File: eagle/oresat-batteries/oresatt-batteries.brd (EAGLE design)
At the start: 160 x 100 mm, 6 parts, among them U1 TCAN330

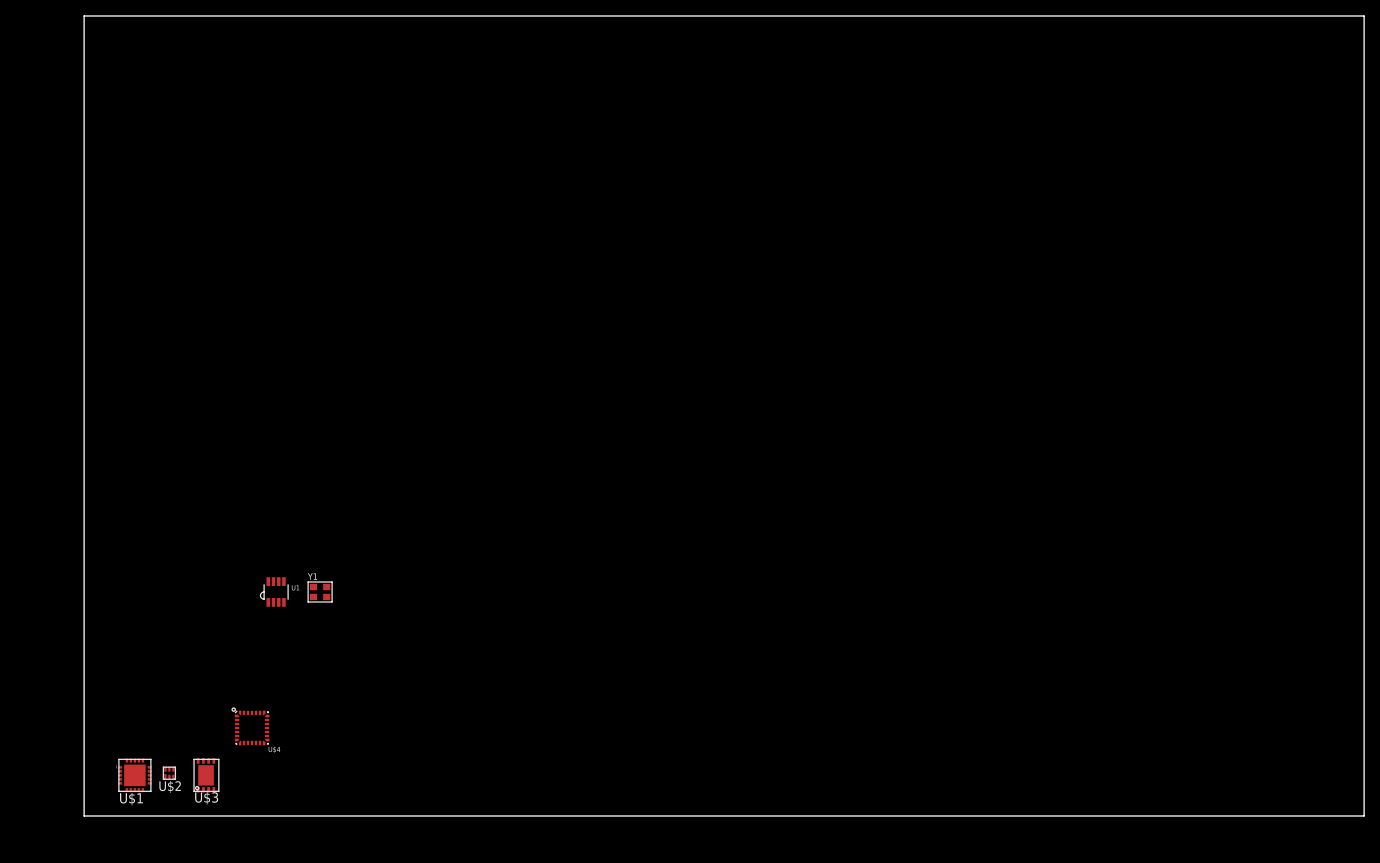
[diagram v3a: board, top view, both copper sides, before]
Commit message: Added 40 pin for real this time.
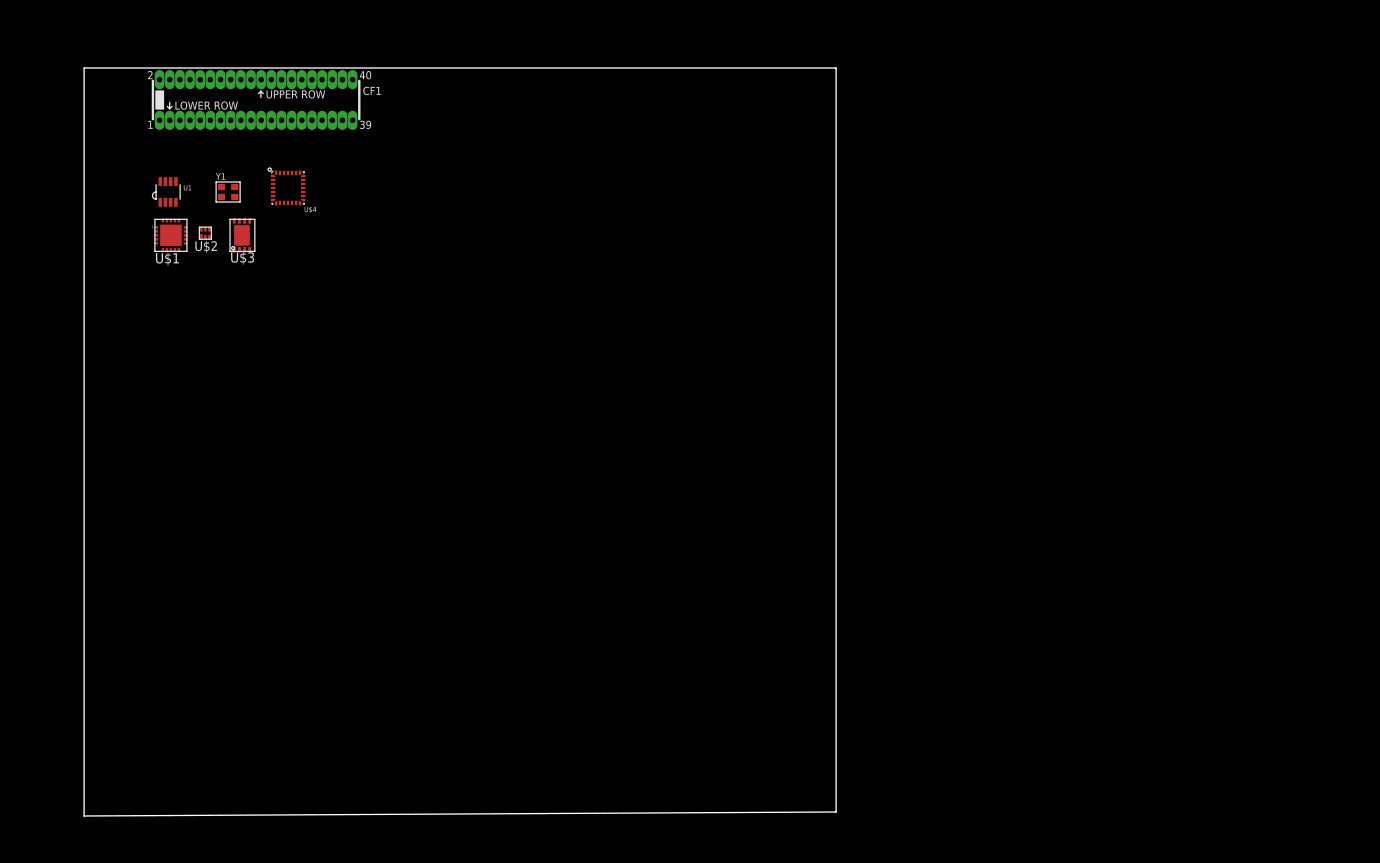
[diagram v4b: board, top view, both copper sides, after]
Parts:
- added CF1: ORESAT-CONNECTOR-40PIN, low-gain-radio:HARWIN-ARCHER-M50-3202045
- moved U$1 67.6 mm to (10.8, 72.6)
- moved U$2 67.6 mm to (15.2, 72.8)
- moved U$3 67.6 mm to (19.7, 72.6)
- moved U$4 67.6 mm to (25.5, 78.5)
- moved U1 51.8 mm to (10.5, 78.0)
- moved Y1 51.3 mm to (18.0, 78.0)
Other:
- board size 160 x 100 mm -> 94 x 93.5 mm
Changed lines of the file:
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@@
 <board>
 <plain>
-<wire x1="0" y1="0" x2="160" y2="0" width="0" layer="20"/>
-<wire x1="160" y1="0" x2="160" y2="100" width="0" layer="20"/>
-<wire x1="160" y1="100" x2="0" y2="100" width="0" layer="20"/>
-<wire x1="0" y1="100" x2="0" y2="0" width="0" layer="20"/>
+<wire x1="0" y1="0" x2="94" y2="0.5" width="0" layer="20"/>
+<wire x1="94" y1="0.5" x2="94" y2="93.5" width="0" layer="20"/>
+<wire x1="94" y1="93.5" x2="0" y2="93.5" width="0" layer="20"/>
+<wire x1="0" y1="93.5" x2="0" y2="0" width="0" layer="20"/>
 </plain>
 <attributes>
@@
 </autorouter>
 <elements>
-<element name="U$1" library="oresat-batteries" package="20_4X4_VVTQ" value="ADP5063" x="6.35" y="5.08"/>
-<element name="U$2" library="oresat-batteries" package="PSOP6" value="BQ2970" x="10.66" y="5.35"/>
-<element name="U$3" library="oresat-batteries" package="WDFN8_3X4" value="LC709203F" x="15.24" y="5.08"/>
-<element name="U$4" library="oresat-batteries" package="UFQFPN-28" value="STM32F042G" x="21" y="11"/>
-<element name="U1" library="oresat-batteries" package="SOT23-8_TI-DCN" value="TCAN330" x="24" y="28"/>
-<element name="Y1" library="low-gain-radio" package="CRYSTAL_2.5X2" value="" x="29.5" y="28"/>
+<element name="U$1" library="oresat-batteries" package="20_4X4_VVTQ" value="ADP5063" x="10.85" y="72.58"/>
+<element name="U$2" library="oresat-batteries" package="PSOP6" value="BQ2970" x="15.16" y="72.85"/>
+<element name="U$3" library="oresat-batteries" package="WDFN8_3X4" value="LC709203F" x="19.74" y="72.58"/>
+<element name="U$4" library="oresat-batteries" package="UFQFPN-28" value="STM32F042G" x="25.5" y="78.5"/>
+<element name="U1" library="oresat-batteries" package="SOT23-8_TI-DCN" value="TCAN330" x="10.5" y="78"/>
+<element name="Y1" library="low-gain-radio" package="CRYSTAL_2.5X2" value="" x="18" y="78"/>
+<element name="CF1" library="low-gain-radio" package="HARWIN-ARCHER-M50-3202045" value="ORESAT-CONNECTOR-40PIN" x="21.5" y="89.5"/>
 </elements>
 <signals>

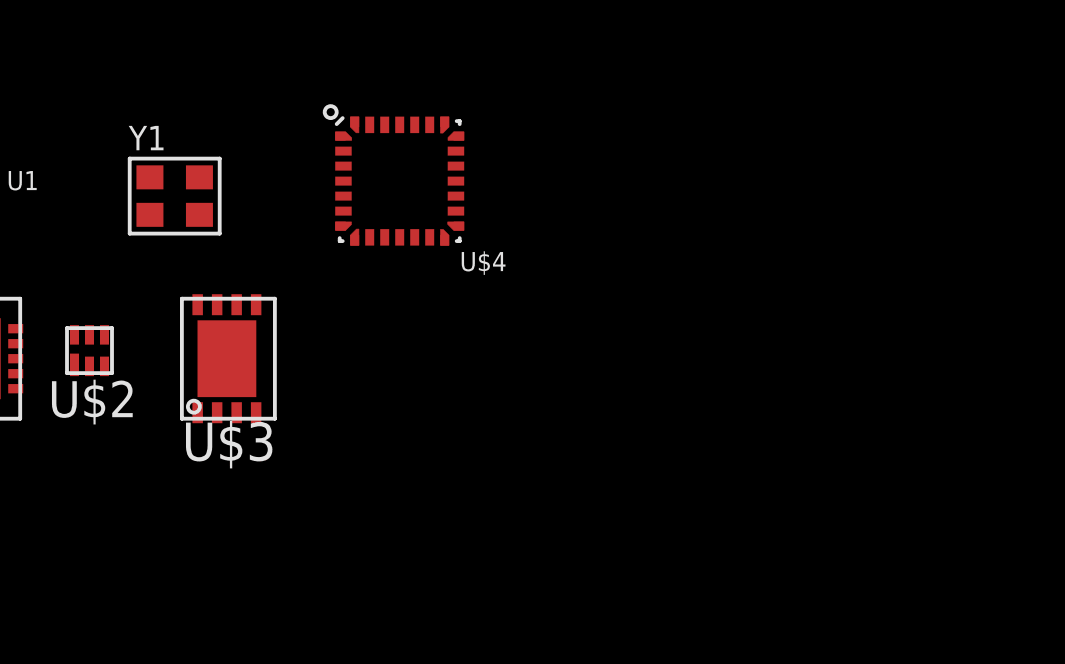
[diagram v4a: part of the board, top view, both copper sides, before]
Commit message: Swapped fuel gauge for ti BQ27500
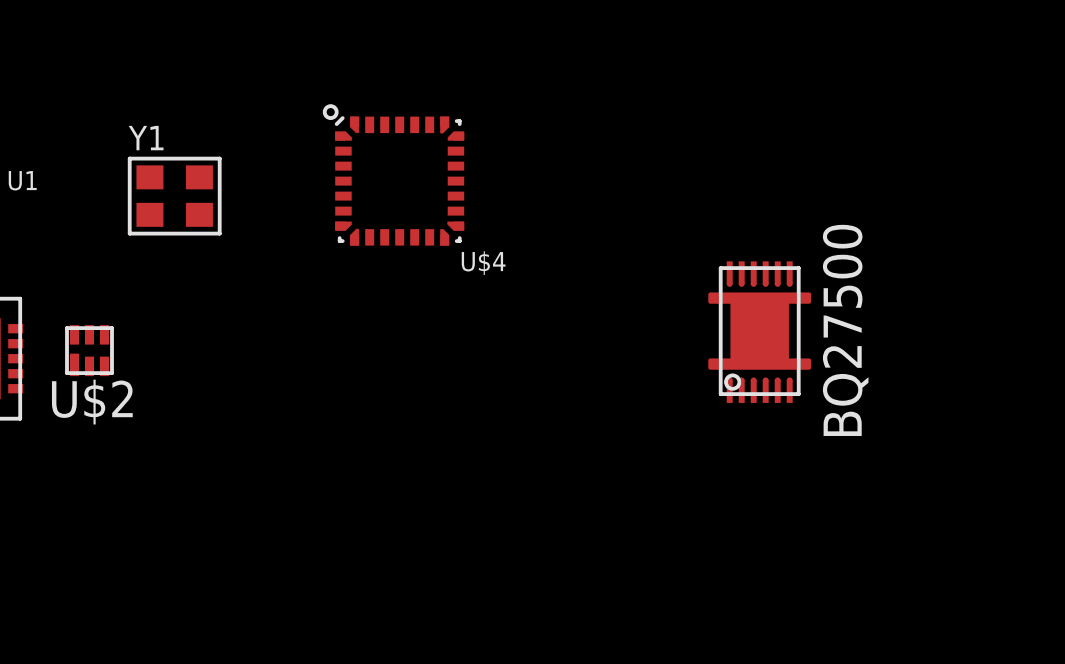
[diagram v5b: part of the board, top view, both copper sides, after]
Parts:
- U$3: value LC709203F -> BQ27500; device oresat-batteries:WDFN8_3X4 -> oresat-batteries:S-PDSO-N12
- moved U$3 17.8 mm to (37.5, 73.5)
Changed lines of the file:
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@@
 <element name="U$1" library="oresat-batteries" package="20_4X4_VVTQ" value="ADP5063" x="10.85" y="72.58"/>
 <element name="U$2" library="oresat-batteries" package="PSOP6" value="BQ2970" x="15.16" y="72.85"/>
-<element name="U$3" library="oresat-batteries" package="WDFN8_3X4" value="LC709203F" x="19.74" y="72.58"/>
 <element name="U$4" library="oresat-batteries" package="UFQFPN-28" value="STM32F042G" x="25.5" y="78.5"/>
 <element name="U1" library="oresat-batteries" package="SOT23-8_TI-DCN" value="TCAN330" x="10.5" y="78"/>
 <element name="Y1" library="low-gain-radio" package="CRYSTAL_2.5X2" value="" x="18" y="78"/>
 <element name="CF1" library="low-gain-radio" package="HARWIN-ARCHER-M50-3202045" value="ORESAT-CONNECTOR-40PIN" x="21.5" y="89.5"/>
+<element name="U$3" library="oresat-batteries" package="S-PDSO-N12" value="BQ27500" x="37.5" y="73.5"/>
 </elements>
 <signals>

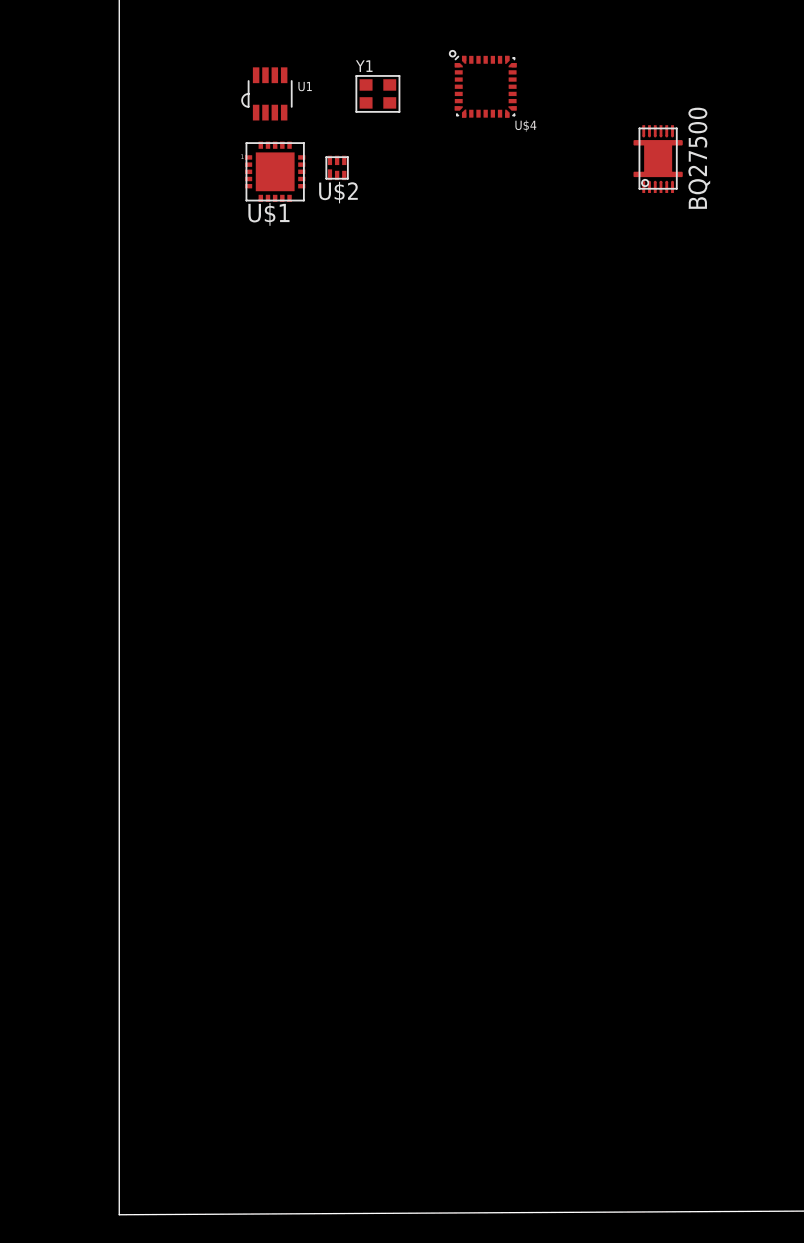
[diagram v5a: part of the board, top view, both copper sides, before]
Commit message: Replaced BQ27500 with STC300lST
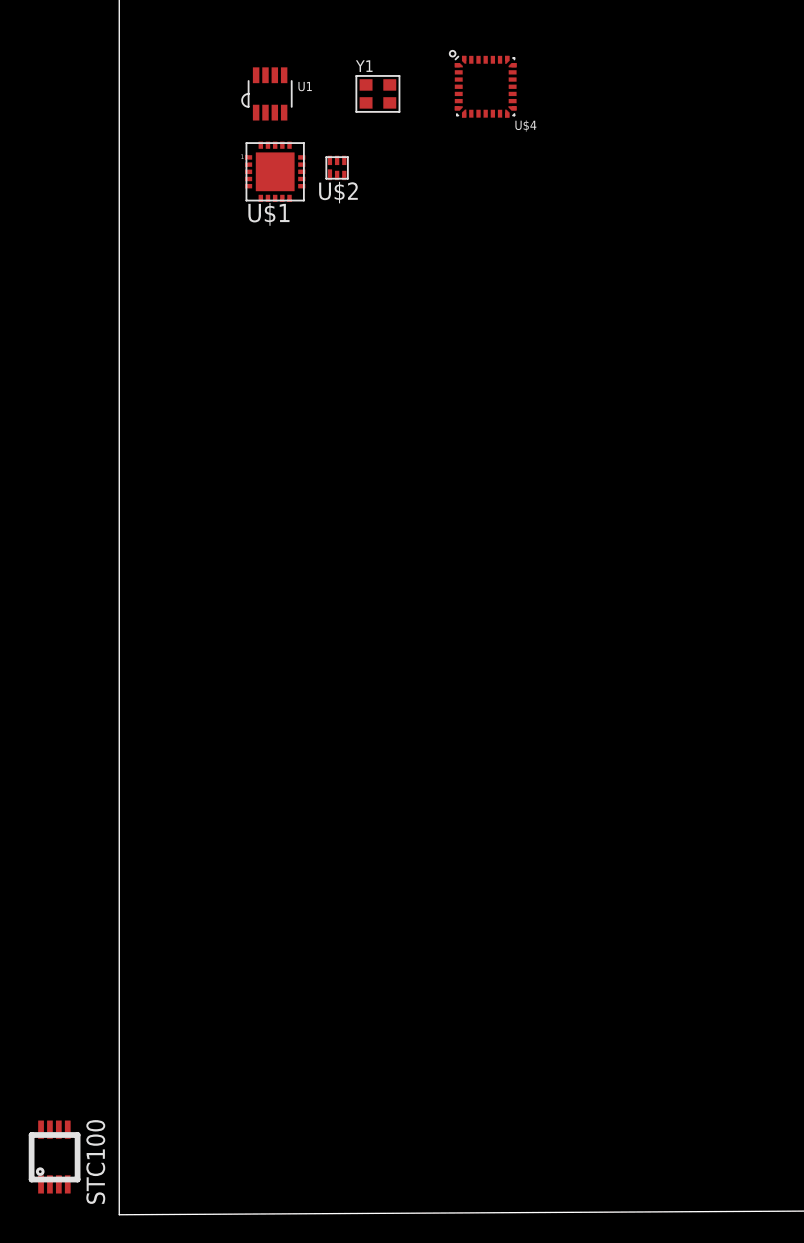
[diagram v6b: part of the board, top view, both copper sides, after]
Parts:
- removed U$3: BQ27500, oresat-batteries:S-PDSO-N12
- added U$5: STC3100LST, oresat-batteries:MINISO-8
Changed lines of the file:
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@@
 <element name="Y1" library="low-gain-radio" package="CRYSTAL_2.5X2" value="" x="18" y="78"/>
 <element name="CF1" library="low-gain-radio" package="HARWIN-ARCHER-M50-3202045" value="ORESAT-CONNECTOR-40PIN" x="21.5" y="89.5"/>
-<element name="U$3" library="oresat-batteries" package="S-PDSO-N12" value="BQ27500" x="37.5" y="73.5"/>
+<element name="U$5" library="oresat-batteries" package="MINISO-8" value="STC3100LST" x="-4.5" y="4"/>
 </elements>
 <signals>

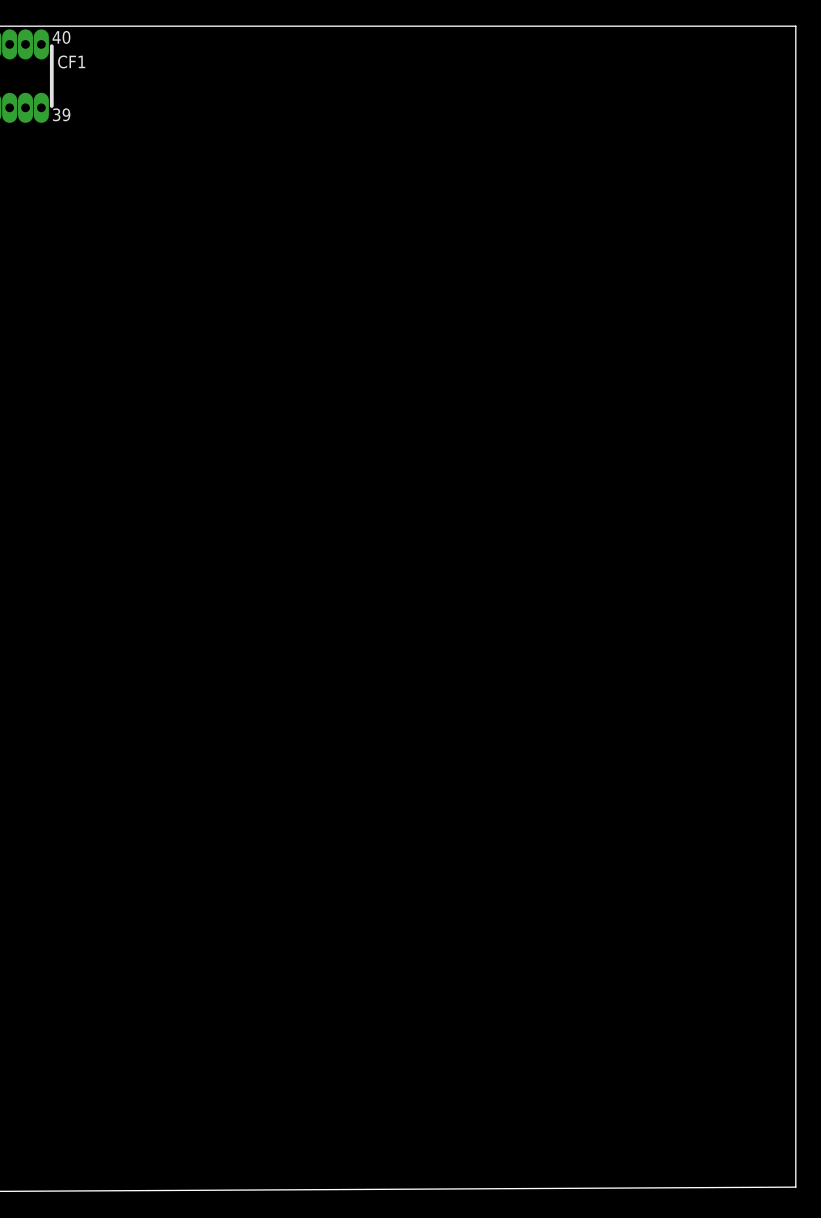
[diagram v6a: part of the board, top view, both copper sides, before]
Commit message: Added potential battery to schematic
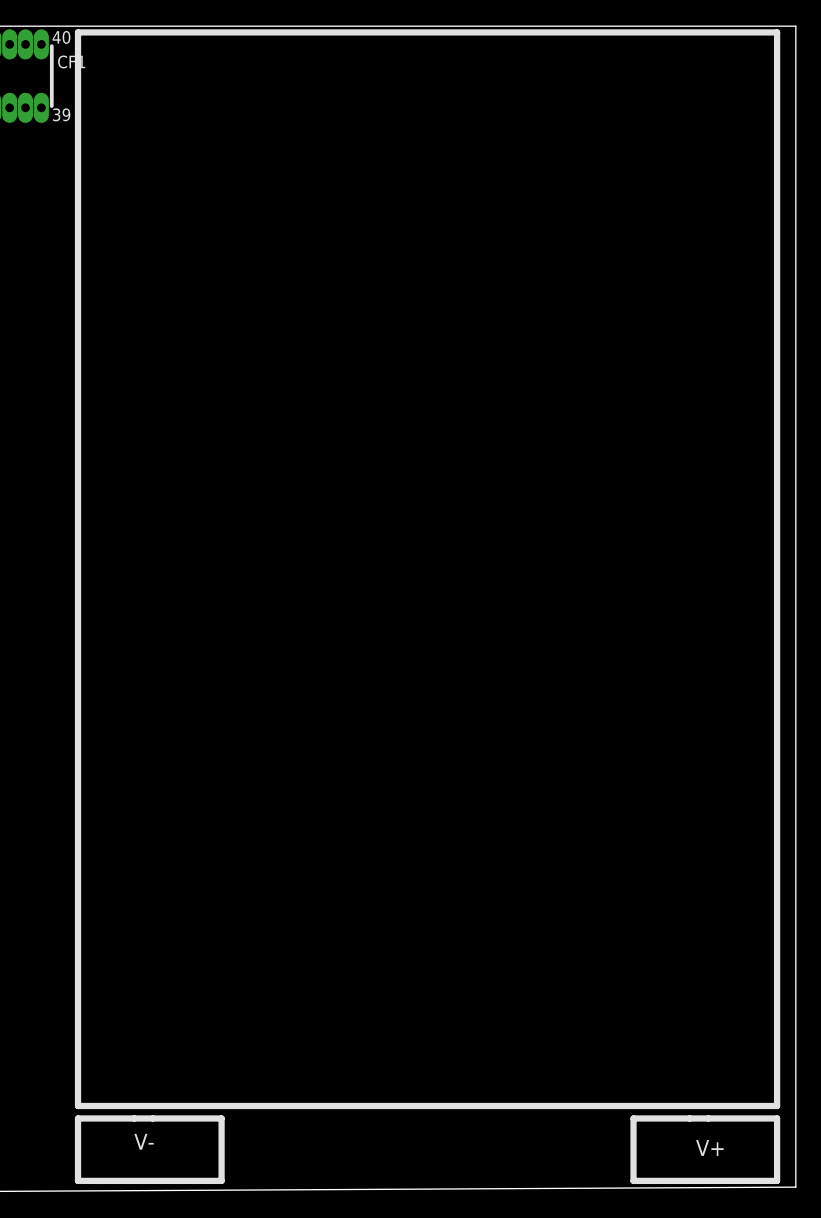
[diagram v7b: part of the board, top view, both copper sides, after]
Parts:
- added U$3: 1.5AHBATT, oresat-batteries:1.5AH
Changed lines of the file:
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@@
 <element name="CF1" library="low-gain-radio" package="HARWIN-ARCHER-M50-3202045" value="ORESAT-CONNECTOR-40PIN" x="21.5" y="89.5"/>
 <element name="U$5" library="oresat-batteries" package="MINISO-8" value="STC3100LST" x="-4.5" y="4"/>
+<element name="U$3" library="oresat-batteries" package="1.5AH" value="1.5AHBATT" x="64.5" y="50"/>
 </elements>
 <signals>
